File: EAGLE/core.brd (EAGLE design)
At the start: 20.3 x 35.6 mm, 47 parts, among them IC1 MCP1825S-3302E, Q1 MMDT3904, U2 STM32F10XCXT6, U3 SST25VF040B-S2, U4 NL17SZ125SOT553, X1 USB-MICROB, X2 IPEX-20279-001E, Y1 32Khz, Y2 8Mhz

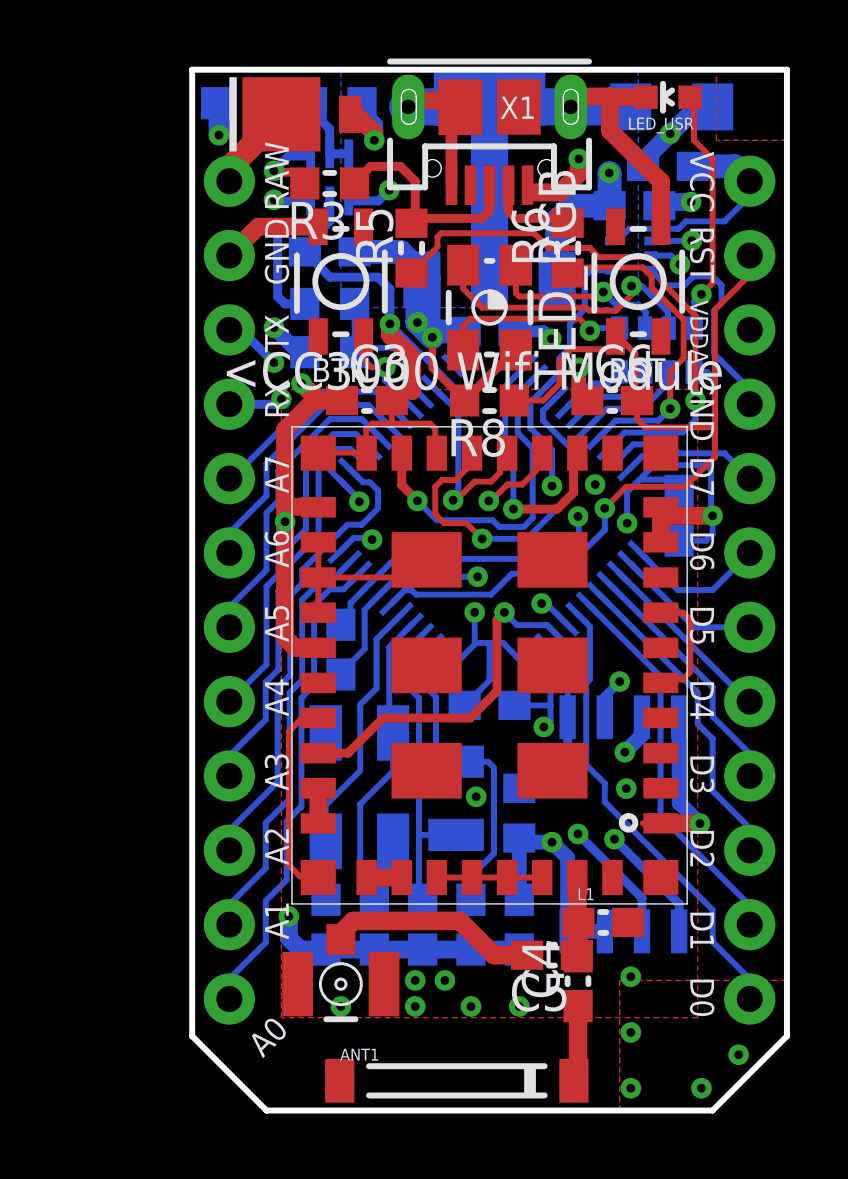
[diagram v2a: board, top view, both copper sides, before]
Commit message: Quick schematic and layout for rf-v3
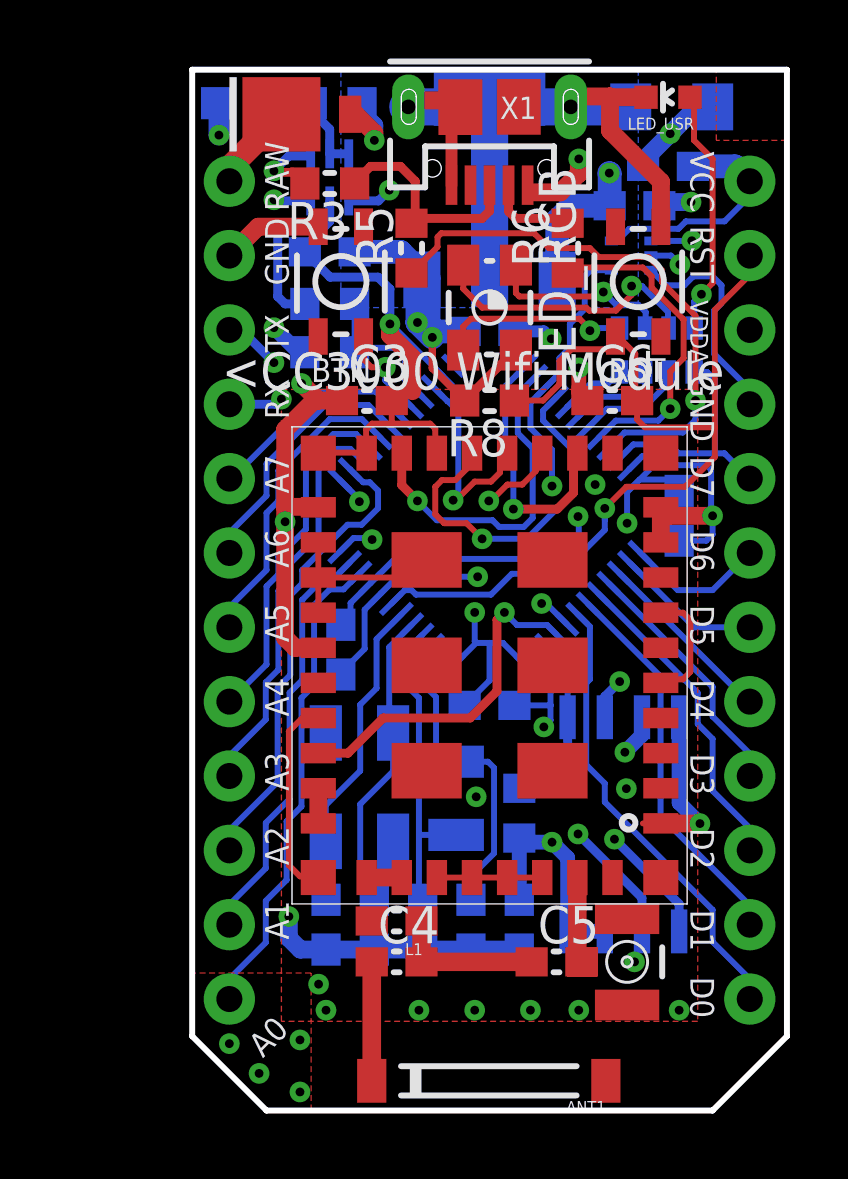
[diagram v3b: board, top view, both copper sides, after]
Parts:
- moved X2 9.81 mm to (14.9, 5.08), turned to 90 degrees
- moved L1 7.06 mm to (6.99, 6.48), turned to 180 degrees
- moved C4 6.23 mm to (6.99, 5.08), turned to 0 degrees
- moved ANT1 1.09 mm to (10.1, 1.02), turned to 180 degrees
- moved C5 0.27 mm to (12.4, 5.08), turned to 0 degrees
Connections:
- removed net N$5: C4.2, C5.1, L1.1, U1.RF_ANT
- new net N$4: C4.2, C5.1, L1.1
- net N$2: now also U1.RF_ANT
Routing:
- net N$4: track 0.00 -> 5.16 mm
- net N$2: track 7.23 -> 2.94 mm
- net N$5: track 2.74 -> 0.00 mm
- net N$3: track 2.61 -> 4.06 mm
- net GND: vias 26 -> 27
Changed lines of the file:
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@@
 <layer number="29" name="tStop" color="7" fill="3" visible="no" active="yes"/>
 <layer number="30" name="bStop" color="7" fill="6" visible="no" active="yes"/>
-<layer number="31" name="tCream" color="7" fill="4" visible="no" active="yes"/>
+<layer number="31" name="tCream" color="7" fill="4" visible="yes" active="yes"/>
 <layer number="32" name="bCream" color="7" fill="5" visible="no" active="yes"/>
 <layer number="33" name="tFinish" color="6" fill="3" visible="no" active="yes"/>
@@
 </element>
 <element name="U1" library="CC3000" package="CC3000" value="" x="10.16" y="15.24" locked="yes" smashed="yes" rot="R180"/>
-<element name="C4" library="rcl" package="C0603" value="2.2pF" x="13.1826" y="4.4196" smashed="yes" rot="R90">
-<attribute name="NAME" x="12.5476" y="3.7846" size="1.27" layer="25" rot="R90"/>
-<attribute name="VALUE" x="12.5476" y="3.937" size="0.4064" layer="27" rot="R180"/>
+<element name="C4" library="rcl" package="C0603" value="2.2pF" x="6.985" y="5.08" smashed="yes">
+<attribute name="NAME" x="6.35" y="5.715" size="1.27" layer="25"/>
+<attribute name="VALUE" x="6.5024" y="5.715" size="0.4064" layer="27" rot="R90"/>
 </element>
 <element name="C3" library="rcl" package="C0603" value="100nF" x="5.969" y="24.257" locked="yes" smashed="yes">
@@
 <attribute name="VALUE" x="13.7755" y="27.6352" size="0.4064" layer="28" rot="MR180"/>
 </element>
-<element name="X2" library="Spark" package="IPEX-20279-001E" value="IPEX-20279-001E" x="5.08" y="4.318" locked="yes"/>
-<element name="C5" library="rcl" package="C0603" value="10pF" x="12.2936" y="5.3086" smashed="yes" rot="R180">
-<attribute name="NAME" x="12.9286" y="4.6736" size="1.27" layer="25" rot="R180"/>
-<attribute name="VALUE" x="10.6426" y="5.4356" size="0.4064" layer="27" rot="R180"/>
-</element>
-<element name="ANT1" library="Spark" package="AT8010" value="AT8010" x="9.0424" y="1.016" smashed="yes">
-<attribute name="NAME" x="5.0524" y="1.706" size="0.4064" layer="25"/>
+<element name="X2" library="Spark" package="IPEX-20279-001E" value="IPEX-20279-001E" x="14.859" y="5.08" rot="R90"/>
+<element name="ANT1" library="Spark" package="AT8010" value="AT8010" x="10.1346" y="1.016" smashed="yes" rot="R180">
+<attribute name="NAME" x="14.1246" y="0.326" size="0.4064" layer="25" rot="R180"/>
 </element>
 <element name="C15" library="Spark" package="EIA3216" value="10uF" x="16.383" y="34.29" locked="yes" smashed="yes" rot="MR180">
@@
 </element>
 <element name="D1" library="Spark" package="DIODE-DO-220AA(SMP)" value="DIODE" x="3.048" y="34.036" locked="yes"/>
-<element name="L1" library="SparkFun-Passives" package="0603" value="2.2nH" x="14.0462" y="6.4262"/>
+<element name="L1" library="SparkFun-Passives" package="0603" value="2.2nH" x="6.985" y="6.477" rot="R180"/>
 <element name="U4" library="Spark" package="SOT-553" value="NL17SZ125SOT553" x="15.6718" y="29.21" rot="MR270"/>
+<element name="C5" library="rcl" package="C0603" value="10pF" x="12.446" y="5.08"/>
 </elements>
 <signals>
@@
 <vertex x="0" y="35.56"/>
 <vertex x="20.32" y="35.56"/>
-<vertex x="20.447" y="3.175"/>
-<vertex x="0.127" y="3.175"/>
+<vertex x="20.447" y="3.048"/>
+<vertex x="0.127" y="3.048"/>
 </polygon>
 <contactref element="U1" pad="GND@39"/>
@@
 <contactref element="X2" pad="2@1"/>
 <contactref element="X2" pad="2@2"/>
-<via x="5.08" y="3.556" extent="1-16" drill="0.3"/>
-<via x="7.62" y="3.556" extent="1-16" drill="0.3"/>
-<via x="9.525" y="3.556" extent="1-16" drill="0.3"/>
-<via x="11.176" y="3.556" extent="1-16" drill="0.3"/>
+<via x="3.683" y="0.635" extent="1-16" drill="0.3"/>
+<via x="9.652" y="3.429" extent="1-16" drill="0.3"/>
+<via x="13.208" y="3.429" extent="1-16" drill="0.3"/>
+<via x="16.637" y="3.429" extent="1-16" drill="0.3"/>
 <polygon width="0.1524" layer="1" thermals="no">
-<vertex x="3.048" y="3.175"/>
+<vertex x="3.048" y="3.048"/>
 <vertex x="3.048" y="24.638"/>
 <vertex x="17.272" y="24.638"/>
-<vertex x="17.272" y="3.175"/>
+<vertex x="17.272" y="3.048"/>
 </polygon>
 <contactref element="C15" pad="C"/>
@@
 <via x="0.9144" y="33.3248" extent="1-16" drill="0.3"/>
 <contactref element="L1" pad="2"/>
-<via x="14.986" y="2.667" extent="1-16" drill="0.3"/>
-<via x="14.986" y="4.572" extent="1-16" drill="0.3"/>
+<via x="15.113" y="5.08" extent="1-16" drill="0.3"/>
 <contactref element="U1" pad="GND@11"/>
 <contactref element="U1" pad="GND@16"/>
@@
 <via x="9.7028" y="10.7188" extent="1-16" drill="0.3"/>
 <via x="14.8336" y="10.9982" extent="1-16" drill="0.3"/>
-<polygon width="0.254" layer="1" thermals="no">
-<vertex x="14.605" y="4.445"/>
-<vertex x="14.605" y="0"/>
-<vertex x="17.78" y="0"/>
-<vertex x="20.32" y="2.54"/>
-<vertex x="20.32" y="4.445"/>
-</polygon>
-<polygon width="0.254" layer="2" thermals="no">
-<vertex x="14.605" y="4.445"/>
-<vertex x="14.605" y="0"/>
-<vertex x="17.78" y="0"/>
-<vertex x="20.32" y="2.54"/>
-<vertex x="20.32" y="4.445"/>
-</polygon>
-<via x="8.636" y="4.445" extent="1-16" drill="0.3"/>
-<via x="7.62" y="4.445" extent="1-16" drill="0.3"/>
-<via x="14.986" y="0.762" extent="1-16" drill="0.3"/>
-<via x="17.399" y="0.762" extent="1-16" drill="0.3"/>
-<via x="18.669" y="1.905" extent="1-16" drill="0.3"/>
+<via x="11.557" y="3.429" extent="1-16" drill="0.3"/>
+<via x="4.318" y="4.318" extent="1-16" drill="0.3"/>
 <wire x1="15.506" y1="34.6202" x2="14.3002" y2="34.6202" width="0.6096" layer="1"/>
 <wire x1="14.3002" y1="34.6202" x2="14.2748" y2="34.6456" width="0.6096" layer="1"/>
+<polygon width="0.1524" layer="1" thermals="no">
+<vertex x="0" y="4.699"/>
+<vertex x="0" y="2.54"/>
+<vertex x="2.54" y="0"/>
+<vertex x="4.064" y="0"/>
+<vertex x="4.064" y="4.699"/>
+</polygon>
+<polygon width="0.1524" layer="2" thermals="no">
+<vertex x="0" y="4.699"/>
+<vertex x="0" y="2.54"/>
+<vertex x="2.54" y="0"/>
+<vertex x="4.064" y="0"/>
+<vertex x="4.064" y="4.699"/>
+</polygon>
+<via x="7.747" y="3.429" extent="1-16" drill="0.3"/>
+<via x="4.572" y="3.429" extent="1-16" drill="0.3"/>
+<via x="3.683" y="2.413" extent="1-16" drill="0.3"/>
+<via x="1.27" y="2.286" extent="1-16" drill="0.3"/>
+<via x="2.286" y="1.27" extent="1-16" drill="0.3"/>
 </signal>
 <signal name="RAW" class="1">
@@
 </signal>
 <signal name="N$2" class="2">
+<contactref element="X2" pad="1"/>
+<contactref element="U1" pad="RF_ANT"/>
 <contactref element="C5" pad="2"/>
-<contactref element="X2" pad="1"/>
-<wire x1="5.4991" y1="6.477" x2="5.08" y2="6.0579" width="0.635" layer="1"/>
-<wire x1="5.08" y1="6.0579" x2="5.08" y2="5.8455" width="0.635" layer="1"/>
-<wire x1="11.4436" y1="5.3086" x2="10.3124" y2="5.3086" width="0.635" layer="1"/>
-<wire x1="10.3124" y1="5.3086" x2="9.144" y2="6.477" width="0.635" layer="1"/>
-<wire x1="9.144" y1="6.477" x2="5.4991" y2="6.477" width="0.635" layer="1"/>
-</signal>
-<signal name="N$5" class="2">
-<contactref element="C4" pad="2"/>
-<contactref element="U1" pad="RF_ANT"/>
-<contactref element="C5" pad="1"/>
-<wire x1="13.1826" y1="5.2696" x2="13.1436" y2="5.3086" width="0.635" layer="1"/>
-<contactref element="L1" pad="1"/>
-<wire x1="13.16" y1="7.96" x2="13.16" y2="6.4624" width="0.635" layer="1"/>
-<wire x1="13.16" y1="6.4624" x2="13.1962" y2="6.4262" width="0.635" layer="1"/>
-<wire x1="13.1962" y1="6.4262" x2="13.1962" y2="5.3612" width="0.635" layer="1"/>
-<wire x1="13.1962" y1="5.3612" x2="13.1436" y2="5.3086" width="0.635" layer="1"/>
+<wire x1="13.16" y1="7.96" x2="13.16" y2="5.216" width="0.635" layer="1"/>
+<wire x1="13.16" y1="5.216" x2="13.296" y2="5.08" width="0.635" layer="1"/>
+<wire x1="13.296" y1="5.08" x2="13.3315" y2="5.08" width="0" layer="19" extent="1-1"/>
 </signal>
 <signal name="LED1">
@@
 <contactref element="C4" pad="1"/>
 <contactref element="ANT1" pad="SIG"/>
-<wire x1="13.1826" y1="3.5696" x2="13.1826" y2="1.1562" width="0.635" layer="1"/>
-<wire x1="13.1826" y1="1.1562" x2="13.0424" y2="1.016" width="0.635" layer="1"/>
+<wire x1="6.135" y1="5.08" x2="6.135" y2="1.0164" width="0.635" layer="1"/>
+<wire x1="6.135" y1="1.0164" x2="6.1346" y2="1.016" width="0.635" layer="1"/>
+</signal>
+<signal name="N$4" class="2">
+<contactref element="C4" pad="2"/>
+<contactref element="L1" pad="1"/>
+<contactref element="C5" pad="1"/>
+<wire x1="11.596" y1="5.08" x2="7.835" y2="5.08" width="0.635" layer="1"/>
+<wire x1="7.835" y1="5.08" x2="7.835" y2="6.477" width="0.635" layer="1"/>
+</signal>
+<signal name="N$5">
 </signal>
 </signals>

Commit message: Clean up design
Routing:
- net GND: vias 27 -> 25
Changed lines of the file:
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@@
 <layer number="29" name="tStop" color="7" fill="3" visible="no" active="yes"/>
 <layer number="30" name="bStop" color="7" fill="6" visible="no" active="yes"/>
-<layer number="31" name="tCream" color="7" fill="4" visible="yes" active="yes"/>
+<layer number="31" name="tCream" color="7" fill="4" visible="no" active="yes"/>
 <layer number="32" name="bCream" color="7" fill="5" visible="no" active="yes"/>
 <layer number="33" name="tFinish" color="6" fill="3" visible="no" active="yes"/>
@@
 <contactref element="X2" pad="2@2"/>
 <via x="3.683" y="0.635" extent="1-16" drill="0.3"/>
-<via x="9.652" y="3.429" extent="1-16" drill="0.3"/>
+<via x="10.414" y="3.429" extent="1-16" drill="0.3"/>
 <via x="13.208" y="3.429" extent="1-16" drill="0.3"/>
 <via x="16.637" y="3.429" extent="1-16" drill="0.3"/>
@@
 <via x="0.9144" y="33.3248" extent="1-16" drill="0.3"/>
 <contactref element="L1" pad="2"/>
-<via x="15.113" y="5.08" extent="1-16" drill="0.3"/>
 <contactref element="U1" pad="GND@11"/>
 <contactref element="U1" pad="GND@16"/>
@@
 <via x="9.7028" y="10.7188" extent="1-16" drill="0.3"/>
 <via x="14.8336" y="10.9982" extent="1-16" drill="0.3"/>
-<via x="11.557" y="3.429" extent="1-16" drill="0.3"/>
 <via x="4.318" y="4.318" extent="1-16" drill="0.3"/>
 <wire x1="15.506" y1="34.6202" x2="14.3002" y2="34.6202" width="0.6096" layer="1"/>
@@
 </signal>
 </signals>
+<errors>
+</errors>
 </board>
 </drawing>

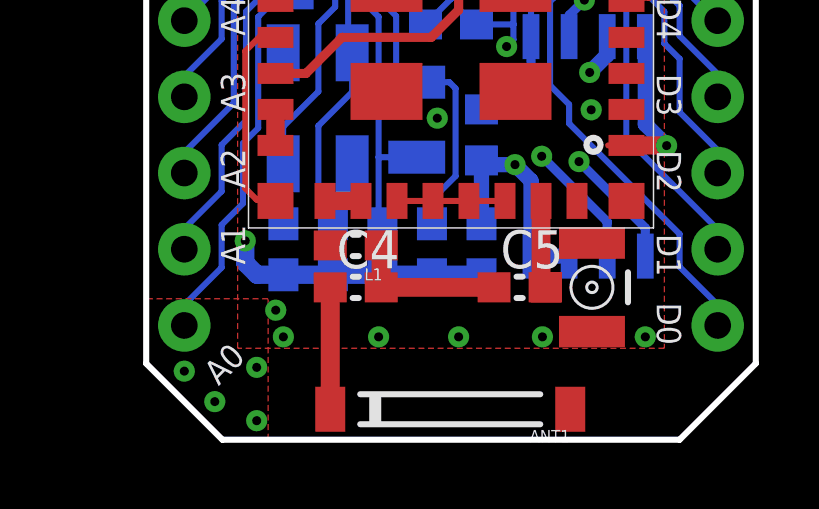
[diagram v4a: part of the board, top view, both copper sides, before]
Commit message: Removed series element and included matching circuit
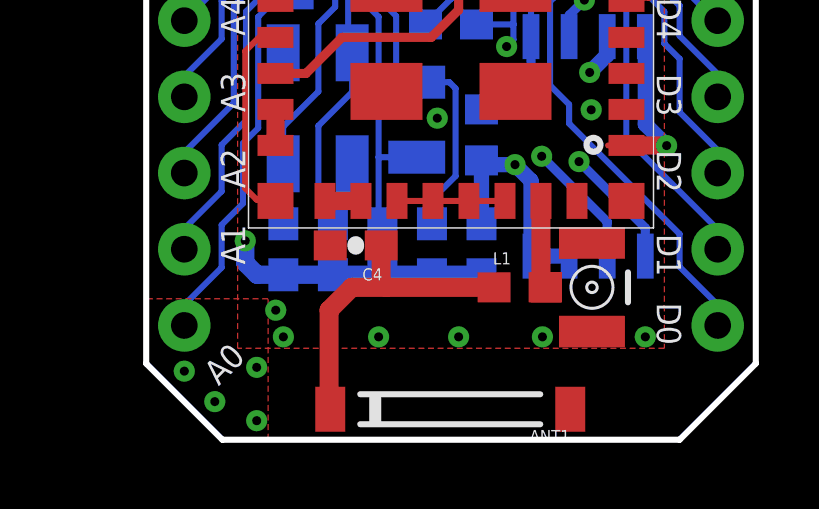
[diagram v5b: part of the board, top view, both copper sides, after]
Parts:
- removed C5: 10pF, rcl:C0603
- C4: value 2.2pF -> 0.8pF; device rcl:C0603 -> SparkFun-Capacitors:0603-CAP
- L1: value 2.2nH -> 3.3nH
- moved L1 5.64 mm to (12.4, 5.08), turned to 0 degrees
- moved C4 1.40 mm to (6.99, 6.48), turned to 180 degrees
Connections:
- removed net N$4: C4.2, C5.1, L1.1
- net GND: now also C4.2; no longer L1.2
- net N$2: now also L1.2; no longer C5.2
- net N$3: now also L1.1
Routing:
- net N$3: track 4.06 -> 10.6 mm
- net N$4: track 5.16 -> 0.00 mm
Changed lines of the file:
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@@
 <?xml version="1.0" encoding="utf-8"?>
 <!DOCTYPE eagle SYSTEM "eagle.dtd">
-<eagle version="6.4">
+<eagle version="6.5.0">
 <drawing>
 <settings>
@@
 <param name="PrefDir.13" value="0"/>
 <param name="PrefDir.14" value="0"/>
-<param name="PrefDir.15" value="*"/>
+<param name="PrefDir.15" value="0"/>
 <param name="PrefDir.16" value="*"/>
 <param name="cfVia" value="8"/>
@@
 </element>
 <element name="U1" library="CC3000" package="CC3000" value="" x="10.16" y="15.24" locked="yes" smashed="yes" rot="R180"/>
-<element name="C4" library="rcl" package="C0603" value="2.2pF" x="6.985" y="5.08" smashed="yes">
-<attribute name="NAME" x="6.35" y="5.715" size="1.27" layer="25"/>
-<attribute name="VALUE" x="6.5024" y="5.715" size="0.4064" layer="27" rot="R90"/>
-</element>
 <element name="C3" library="rcl" package="C0603" value="100nF" x="5.969" y="24.257" locked="yes" smashed="yes">
 <attribute name="NAME" x="5.334" y="24.892" size="1.27" layer="25"/>
@@
 </element>
 <element name="D1" library="Spark" package="DIODE-DO-220AA(SMP)" value="DIODE" x="3.048" y="34.036" locked="yes"/>
-<element name="L1" library="SparkFun-Passives" package="0603" value="2.2nH" x="6.985" y="6.477" rot="R180"/>
+<element name="C4" library="SparkFun-Capacitors" package="0603-CAP" value="0.8pF" x="6.985" y="6.477" rot="R180"/>
 <element name="U4" library="Spark" package="SOT-553" value="NL17SZ125SOT553" x="15.6718" y="29.21" rot="MR270"/>
-<element name="C5" library="rcl" package="C0603" value="10pF" x="12.446" y="5.08"/>
+<element name="L1" library="SparkFun-Passives" package="0603" value="3.3nH" x="12.446" y="5.08"/>
 </elements>
 <signals>
@@
 <wire x1="7.01654375" y1="18.2372" x2="9.7536" y2="18.2372" width="0.2032" layer="16"/>
 <via x="0.9144" y="33.3248" extent="1-16" drill="0.3"/>
-<contactref element="L1" pad="2"/>
+<contactref element="C4" pad="2"/>
 <contactref element="U1" pad="GND@11"/>
 <contactref element="U1" pad="GND@16"/>
@@
 <contactref element="X2" pad="1"/>
 <contactref element="U1" pad="RF_ANT"/>
-<contactref element="C5" pad="2"/>
+<contactref element="L1" pad="2"/>
 <wire x1="13.16" y1="7.96" x2="13.16" y2="5.216" width="0.635" layer="1"/>
 <wire x1="13.16" y1="5.216" x2="13.296" y2="5.08" width="0.635" layer="1"/>
@@
 </signal>
 <signal name="N$3" class="2">
+<contactref element="ANT1" pad="SIG"/>
+<wire x1="6.135" y1="1.0164" x2="6.1346" y2="1.016" width="0.635" layer="1"/>
+<contactref element="L1" pad="1"/>
 <contactref element="C4" pad="1"/>
-<contactref element="ANT1" pad="SIG"/>
-<wire x1="6.135" y1="5.08" x2="6.135" y2="1.0164" width="0.635" layer="1"/>
-<wire x1="6.135" y1="1.0164" x2="6.1346" y2="1.016" width="0.635" layer="1"/>
-</signal>
-<signal name="N$4" class="2">
-<contactref element="C4" pad="2"/>
-<contactref element="L1" pad="1"/>
-<contactref element="C5" pad="1"/>
-<wire x1="11.596" y1="5.08" x2="7.835" y2="5.08" width="0.635" layer="1"/>
-<wire x1="7.835" y1="5.08" x2="7.835" y2="6.477" width="0.635" layer="1"/>
+<wire x1="11.596" y1="5.08" x2="8.001" y2="5.08" width="0.635" layer="1"/>
+<wire x1="8.001" y1="5.08" x2="6.858" y2="5.08" width="0.635" layer="1"/>
+<wire x1="6.858" y1="5.08" x2="6.096" y2="4.318" width="0.635" layer="1"/>
+<wire x1="6.096" y1="4.318" x2="6.096" y2="1.0546" width="0.635" layer="1"/>
+<wire x1="6.096" y1="1.0546" x2="6.1346" y2="1.016" width="0.635" layer="1"/>
+<wire x1="7.835" y1="6.477" x2="7.835" y2="5.246" width="0.635" layer="1"/>
+<wire x1="7.835" y1="5.246" x2="8.001" y2="5.08" width="0.635" layer="1"/>
 </signal>
 <signal name="N$5">
